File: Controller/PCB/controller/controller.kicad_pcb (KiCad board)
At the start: 2 copper layers, 99.1 x 99.1 mm, 57 parts, among them J1 nRF24L01_Conn, Q1 S9013, Q2 S9013, Q4 S9013, SW1 SW_SPDT, U1 Joystick, U2 Joystick, U3 LM2940-3.0, U5 LM2940-5.0

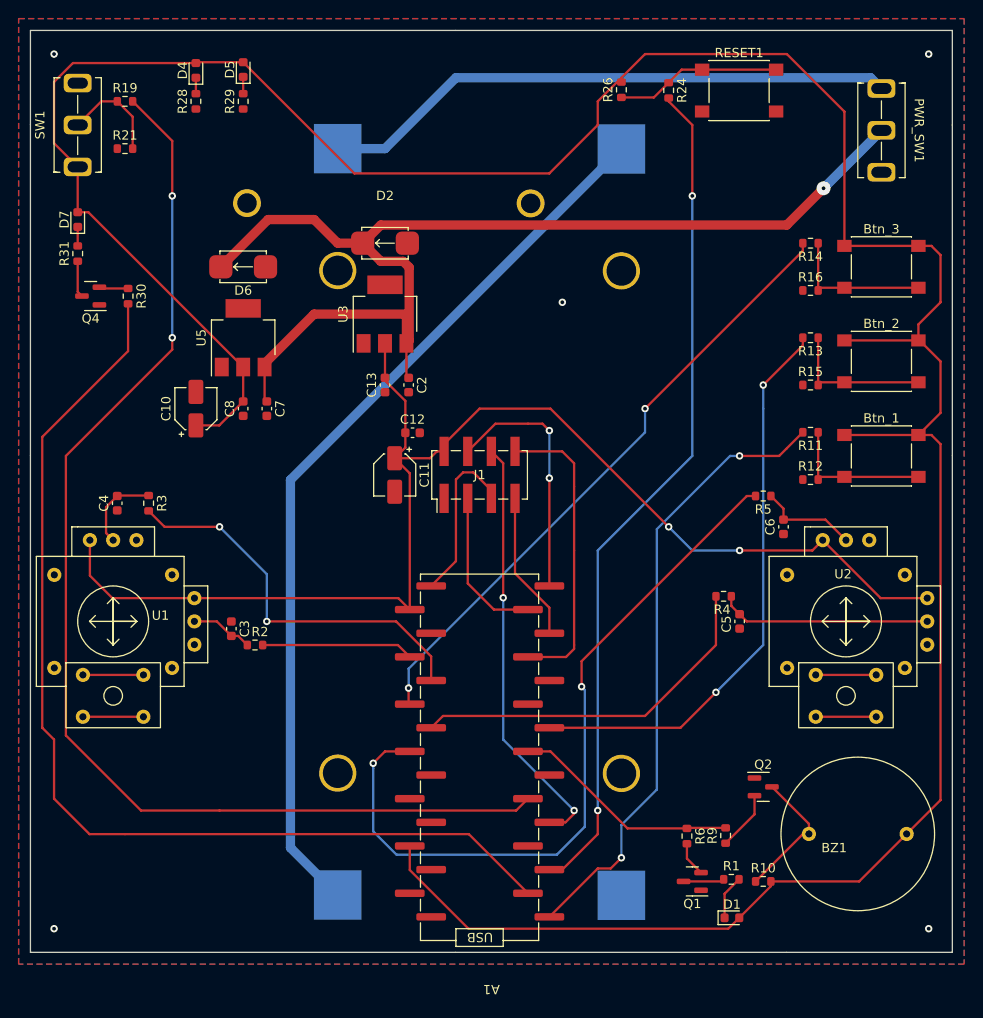
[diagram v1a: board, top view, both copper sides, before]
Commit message: Add Silkscreen notes to PCB
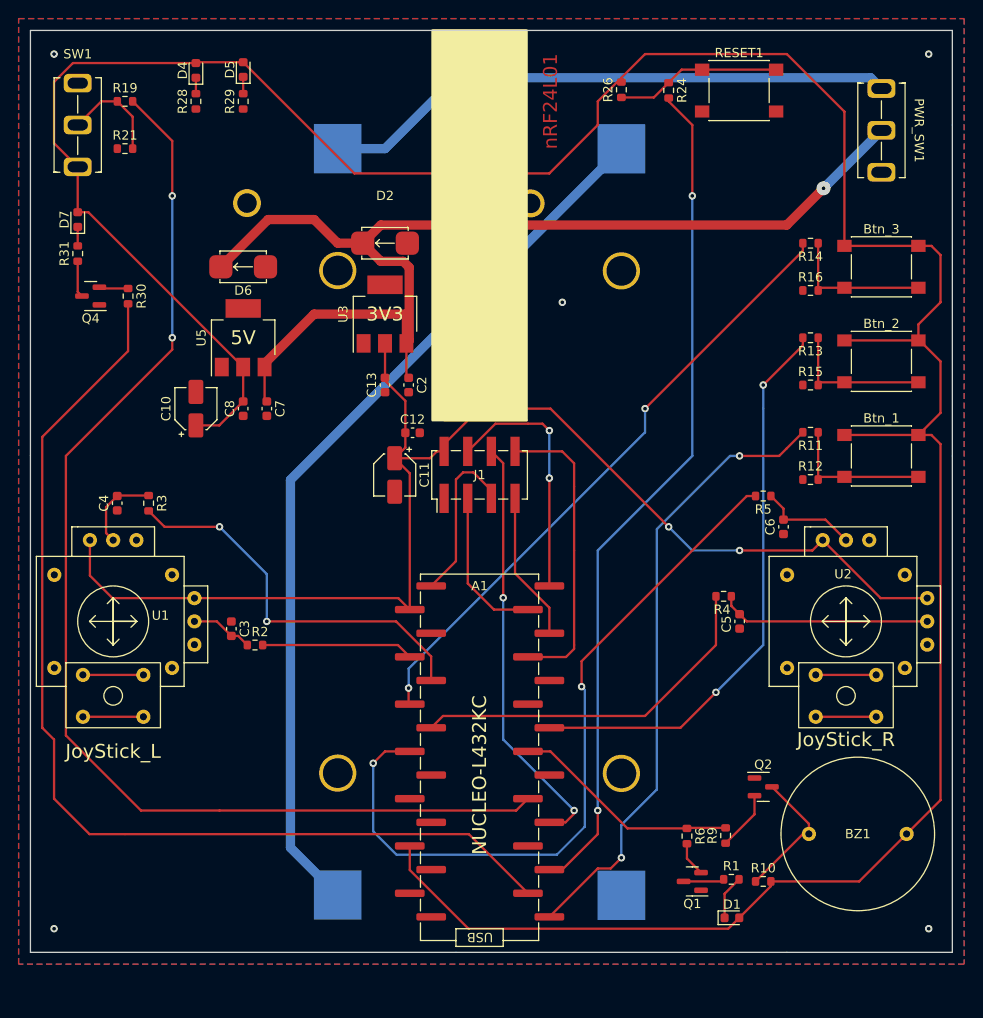
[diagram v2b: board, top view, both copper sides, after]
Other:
- board text added: "3V3"
- board text added: "5V"
- board text added: "JoyStick_L"
- board text added: "JoyStick_R"
- board text added: "NUCLEO-L432KC"
- board text added: "nRF24L01"
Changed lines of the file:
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@@
     (fp_circle (center 0 0) (end 0 -3.81) (layer "F.SilkS") (width 0.12) (fill none))
     (pad "EARTH" thru_hole circle (at -6.325 5) (size 1.524 1.524) (drill 0.762) (layers *.Cu *.Mask)
-      (net 3 "Earth"))
+      (net 3 "Earth") (pintype "passive"))
     (pad "EARTH" thru_hole circle (at -6.325 -5) (size 1.524 1.524) (drill 0.762) (layers *.Cu *.Mask)
-      (net 3 "Earth"))
+      (net 3 "Earth") (pintype "passive"))
     (pad "EARTH" thru_hole circle (at 6.325 -5) (size 1.524 1.524) (drill 0.762) (layers *.Cu *.Mask)
-      (net 3 "Earth"))
+      (net 3 "Earth") (pintype "passive"))
     (pad "EARTH" thru_hole circle (at 6.325 5) (size 1.524 1.524) (drill 0.762) (layers *.Cu *.Mask)
-      (net 3 "Earth"))
+      (net 3 "Earth") (pintype "passive"))
     (pad "SW1" thru_hole circle (at 3.25 5.75) (size 1.524 1.524) (drill 0.762) (layers *.Cu *.Mask)
       (net 44 "unconnected-(U1-PadSW1)") (pintype "bidirectional+no_connect"))
@@
     (property "Sheetname" "")
     (attr smd)
-    (fp_text reference "A1" (at 0 -15.4 180 unlocked) (layer "F.SilkS")
+    (fp_text reference "A1" (at 1.27 27.94 unlocked) (layer "F.SilkS")
       (effects (font (size 1 1) (thickness 0.15)))
     )
@@
     (property "Sheetname" "")
     (attr through_hole)
-    (fp_text reference "BZ1" (at 2.54 -1.5 unlocked) (layer "F.SilkS")
+    (fp_text reference "BZ1" (at 0 0 unlocked) (layer "F.SilkS")
       (effects (font (size 1 1) (thickness 0.15)))
     )
@@
     (fp_circle (center 0 8) (end 1 8) (layer "F.SilkS") (width 0.12) (fill none))
     (pad "EARTH" thru_hole circle (at 6.325 5) (size 1.524 1.524) (drill 0.762) (layers *.Cu *.Mask)
-      (net 3 "Earth"))
+      (net 3 "Earth") (pintype "passive"))
     (pad "EARTH" thru_hole circle (at 6.325 -5) (size 1.524 1.524) (drill 0.762) (layers *.Cu *.Mask)
-      (net 3 "Earth"))
+      (net 3 "Earth") (pintype "passive"))
     (pad "EARTH" thru_hole circle (at -6.325 5) (size 1.524 1.524) (drill 0.762) (layers *.Cu *.Mask)
-      (net 3 "Earth"))
+      (net 3 "Earth") (pintype "passive"))
     (pad "EARTH" thru_hole circle (at -6.325 -5) (size 1.524 1.524) (drill 0.762) (layers *.Cu *.Mask)
-      (net 3 "Earth"))
+      (net 3 "Earth") (pintype "passive"))
     (pad "SW1" thru_hole circle (at 3.25 5.75) (size 1.524 1.524) (drill 0.762) (layers *.Cu *.Mask)
       (net 46 "unconnected-(U2-PadSW1)") (pintype "bidirectional+no_connect"))
@@
     (property "Sheetname" "")
     (attr through_hole)
-    (fp_text reference "SW1" (at 0 -4.04 90 unlocked) (layer "F.SilkS")
+    (fp_text reference "SW1" (at 7.62 0 unlocked) (layer "F.SilkS")
       (effects (font (size 1 1) (thickness 0.15)))
     )
@@
       (net 3 "Earth") (pintype "passive"))
   )
+  (gr_rect (start 151.13 92.71) (end 160.02 92.71) (layer "F.Cu") (width 0.2) (fill none))
+  (gr_rect (start 160.02 50.8) (end 149.86 50.8) (layer "F.Cu") (width 0.2) (fill none))
+  (gr_rect (start 149.86 92.71) (end 160.02 50.8) (layer "F.SilkS") (width 0.2) (fill solid))
   (gr_line (start 106.68 96.52) (end 106.68 60.96) (layer "Edge.Cuts") (width 0.1))
   (gr_line (start 205.74 50.8) (end 205.74 60.96) (layer "Edge.Cuts") (width 0.1))
@@
   (gr_line (start 152.4 149.86) (end 187.96 149.86) (layer "Edge.Cuts") (width 0.1))
   (gr_line (start 205.74 96.52) (end 205.74 149.86) (layer "Edge.Cuts") (width 0.1))
+  (gr_text "nRF24L01" (at 162.56 58.42 90) (layer "F.Cu")
+    (effects (font (size 1.5 1.5) (thickness 0.3)))
+  )
+  (gr_text "3V3\n" (at 144.78 81.28) (layer "F.SilkS")
+    (effects (font (size 1.5 1.5) (thickness 0.3)))
+  )
+  (gr_text "NUCLEO-L432KC" (at 154.94 130.81 90) (layer "F.SilkS")
+    (effects (font (size 1.5 1.5) (thickness 0.3)))
+  )
+  (gr_text "JoyStick_R" (at 194.31 127) (layer "F.SilkS")
+    (effects (font (size 1.5 1.5) (thickness 0.3)))
+  )
+  (gr_text "5V\n" (at 129.54 83.82) (layer "F.SilkS")
+    (effects (font (size 1.5 1.5) (thickness 0.3)))
+  )
+  (gr_text "JoyStick_L" (at 115.57 128.27) (layer "F.SilkS")
+    (effects (font (size 1.5 1.5) (thickness 0.3)))
+  )
+  (gr_text "nRF24L01\n" (at 154.94 87.63 90) (layer "F.SilkS")
+    (effects (font (size 1.5 1.5) (thickness 0.3)))
+  )
   (segment (start 117.172778 80.176001) (end 117.172778 85.256001) (width 0.25) (layer "F.Cu") (net 1))
   (segment (start 107.95 125.73) (end 109.22 127) (width 0.25) (layer "F.Cu") (net 1))

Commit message: Add Voltage Checker Circuit to controller board
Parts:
- added C1: 100nF, Capacitor_SMD:C_0603_1608Metric, F.Cu at (118.1, 133.3)
- added C9: 100nF, Capacitor_SMD:C_0603_1608Metric, F.Cu at (124.3, 134.6)
- added D3: RED, LED_SMD:LED_0603_1608Metric, F.Cu at (135.9, 137.2)
- added R17: 100K, Resistor_SMD:R_0603_1608Metric, F.Cu at (127.0, 133.3)
- added R18: 100K, Resistor_SMD:R_0603_1608Metric, F.Cu at (127.0, 137.2)
- added R20: 1K, Resistor_SMD:R_0603_1608Metric, F.Cu at (135.9, 141.0)
- added R7: 20K, Resistor_SMD:R_0603_1608Metric, F.Cu at (120.7, 132.1)
- added R8: 40K, Resistor_SMD:R_0603_1608Metric, F.Cu at (120.7, 135.3)
- added U4: LM741, My_library:741C, F.Cu at (130.8, 134.4)
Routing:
- net BAT_PWR: track 122.1 -> 192.3 mm
- net +5V: track 322.6 -> 355.8 mm, vias 0 -> 2
- net Net-(R7-Pad1): track 0.00 -> 20.7 mm
- net Net-(R17-Pad1): track 0.00 -> 4.38 mm
- net Net-(D3-Pad2): track 0.00 -> 3.68 mm
- net LED_1: track 112.6 -> 110.2 mm, vias 0 -> 2
- net Net-(D3-Pad1): track 0.00 -> 2.20 mm
- net SW_1: track 128.1 -> 127.7 mm, vias 2 -> 4
- net Earth: vias 5 -> 6

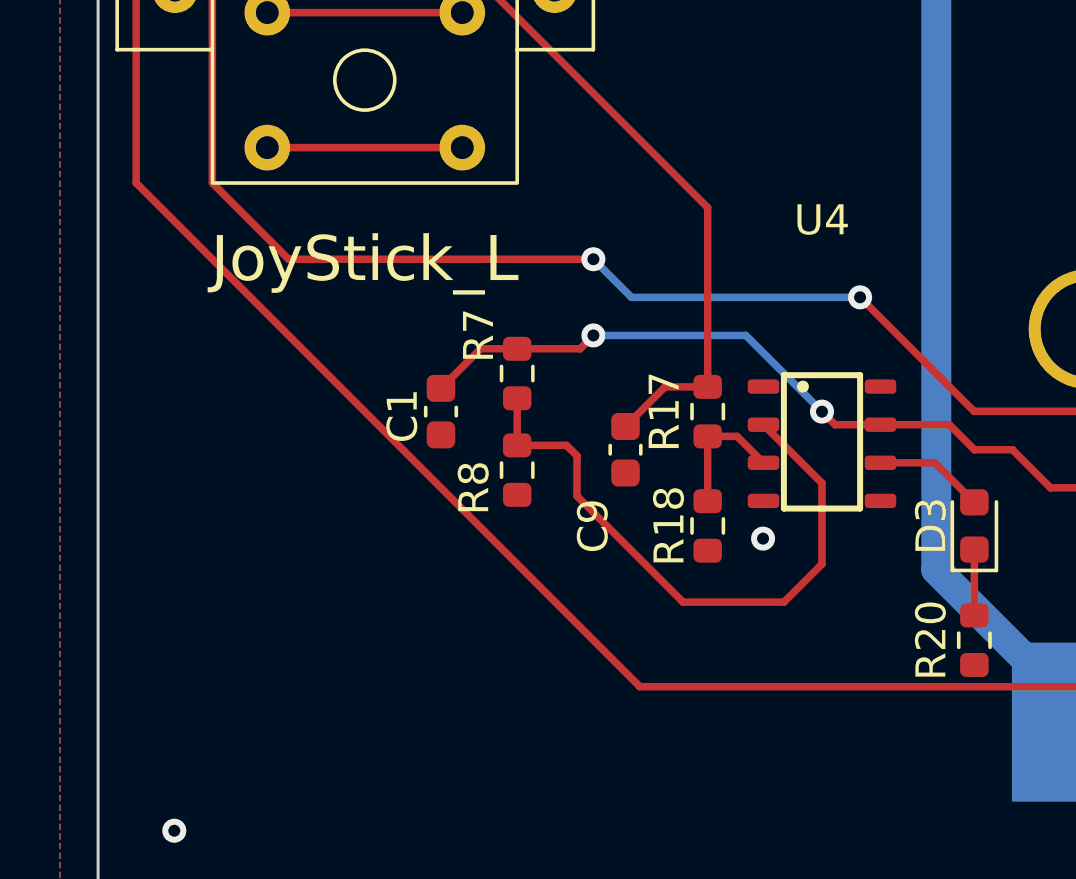
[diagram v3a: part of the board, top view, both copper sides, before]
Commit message: Add Trim pot to battery level checker
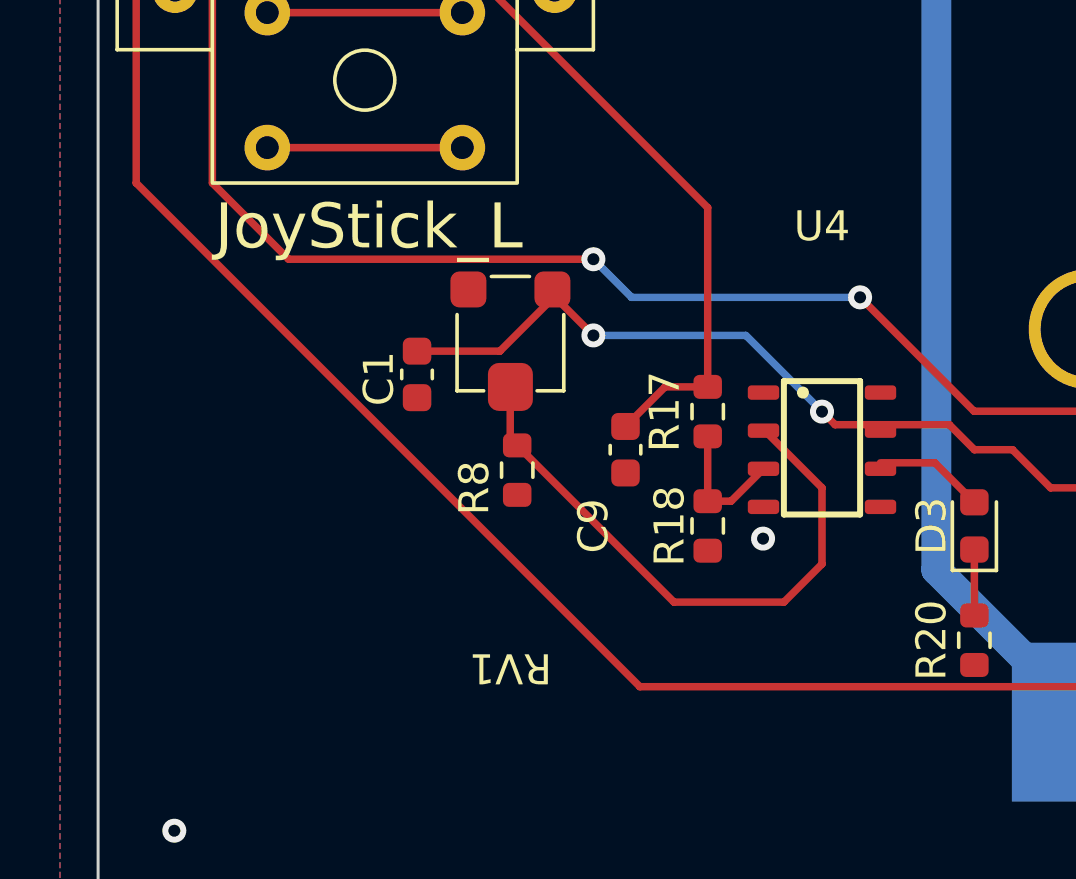
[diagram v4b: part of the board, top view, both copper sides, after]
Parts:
- removed R7: 20K, Resistor_SMD:R_0603_1608Metric
- added RV1: 20K, My_library:35WR100KLFTR, F.Cu at (120.4, 130.9)
- moved C1 1.48 mm to (117.3, 132.1)
- moved U4 0.20 mm to (130.8, 134.6)
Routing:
- net +5V: track 355.8 -> 357.6 mm

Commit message: Create Gerber files
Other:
- board text added: "O.R.C.A - Control Board"
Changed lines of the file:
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@@
       (outputformat 1)
       (mirror false)
-      (drillshape 1)
+      (drillshape 0)
       (scaleselection 1)
       (outputdirectory "")
@@
     (effects (font (size 1.5 1.5) (thickness 0.3)))
   )
+  (gr_text "O.R.C.A - Control Board" (at 123.19 146.05) (layer "F.SilkS")
+    (effects (font (size 1.5 1.5) (thickness 0.3)))
+  )

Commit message: Final PCB for controller along with all build and assembly files
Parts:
- removed C10, C11: 10uF, Capacitor_SMD:CP_Elec_4x5.4
- removed Q4: S9013, Package_TO_SOT_SMD:SOT-23
- added Q3: S9013, Package_TO_SOT_SMD:SOT-23, F.Cu at (113.0, 79.4)
- D1: value RED -> GREEN
- D2, D6: value 1N5817 -> B5817W-5819W; footprint My_library:1N5817M -> Diode_SMD:D_SOD-123
- D3, D4: value RED -> YELLOW
- R1, R11, R13, R14, R19, R20, R24, R28: value 1K -> 2K2
- R29: value 2K -> 1K
- R31: value 390R -> 1K
- U3: value LM2940-3.0 -> ZSR330GTA
- U4: value LM741 -> LM358DR2G; footprint My_library:741C -> Package_SO:SOP-8_3.76x4.96mm_P1.27mm
- U5: value LM2940-5.0 -> ZLDO1117G50TA
- moved D3 3.24 mm to (139.1, 137.8)
- moved R20 3.18 mm to (139.1, 141.0)
- moved U4 2.01 mm to (132.7, 134.0)
- turned D6 to 180 degrees
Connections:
- U4 pad 1: unconnected-(U4-Pad1) -> Net-(D3-Pad2)
- U4 pad 6: Net-(D3-Pad2) -> unconnected-(U4-Pad6)
- U4 pad 7: +5V -> unconnected-(U4-Pad7)
- U4 pad 8: unconnected-(U4-Pad8) -> +5V
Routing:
- net Net-(D3-Pad2): track 3.68 -> 12.4 mm
- net BAT_PWR: track 192.3 -> 186.1 mm
- net Net-(R8-Pad2): track 20.5 -> 23.1 mm
- net +5V: track 357.6 -> 355.1 mm
- net +3V3: track 139.6 -> 138.1 mm
- net Net-(R17-Pad1): track 4.47 -> 5.52 mm
- net Net-(D3-Pad1): track 2.20 -> 1.56 mm
- net SW_1: track 127.7 -> 128.2 mm
- net Earth: vias 6 -> 5
